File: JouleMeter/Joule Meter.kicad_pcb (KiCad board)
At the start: 4 copper layers, 153.8 x 95 mm, 83 parts, among them J1 XT60-M, J2 XT60-M, J3 22035035, J4 22035035, J5 M22-7130442, U1 LMR36510, U3 INA240A1PW, U4 ADS1118IDGS-Q1, U5 MCP6286T-E/OT1, U6 MCP2562

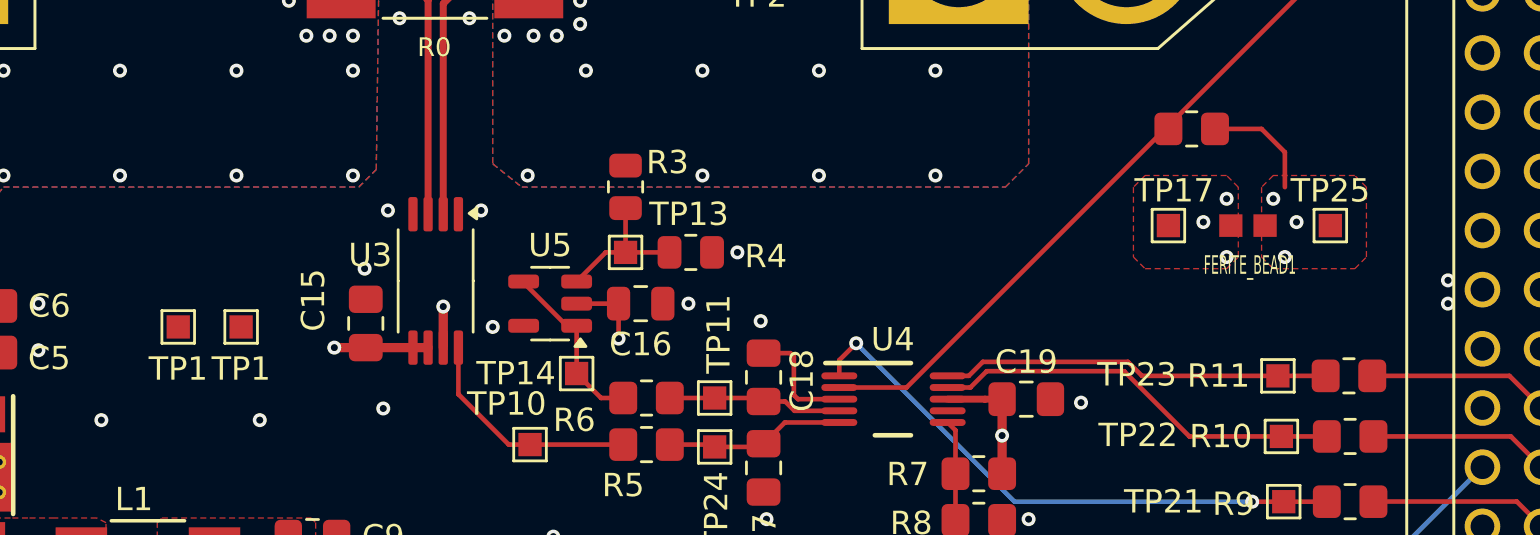
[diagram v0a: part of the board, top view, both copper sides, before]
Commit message: added two new caps next to ferrite bead
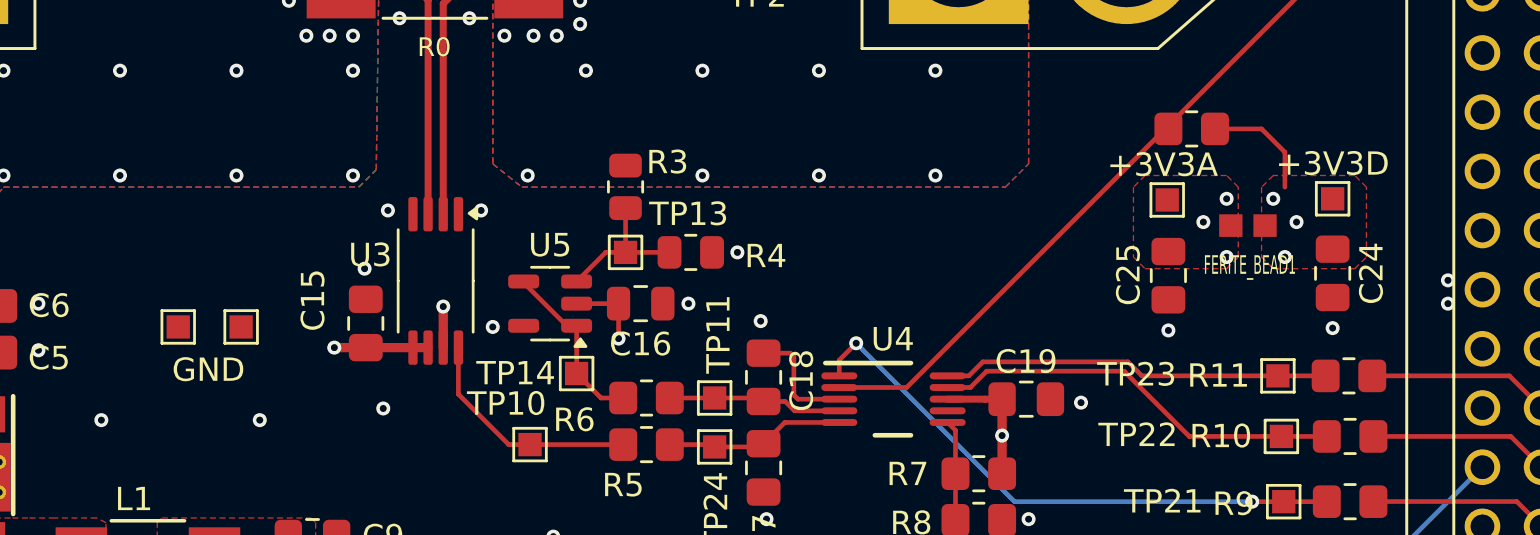
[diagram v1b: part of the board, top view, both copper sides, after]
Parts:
- added C24: 0.1uF, Capacitor_SMD:C_0805_2012Metric_Pad1.18x1.45mm_HandSolder, F.Cu at (137.1, 63.7)
- added C25: 0.1uF, Capacitor_SMD:C_0805_2012Metric_Pad1.18x1.45mm_HandSolder, F.Cu at (130.0, 63.8)
- moved +3V3D 1.15 mm to (137.1, 60.5)
- moved +3V3A 1.10 mm to (129.9, 60.5)
- renumbered TP17 to +3V3A, TP25 to +3V3D, TP1 to GND
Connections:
- C1 pad 3: GND -> (no net)
- C1 pad 4: Net-(J1-POS) -> (no net)
- C3 pad 3: Net-(J2-POS) -> (no net)
- C3 pad 4: GND -> (no net)
- U1 pad 10: GND -> (no net)
- U1 pad 11: GND -> (no net)
- U1 pad 12: GND -> (no net)
- U1 pad 13: GND -> (no net)
- U1 pad 14: GND -> (no net)
- U1 pad 15: GND -> (no net)
- U1 pad 16: GND -> (no net)
- U1 pad 17: GND -> (no net)
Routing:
- net GND: vias 171 -> 173

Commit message: Final Touch Up, Silk Screen
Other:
- board text added: "CAN-N"
- board text added: "CAN-P"
- board text added: "High Power Joulemeter (w/Shunt Resistor) May 2026 University of California, Los Angeles Designed By Sergio Gonzalez"
- board text added: "Special Thanks to: Soloman Ta Edwin Tang For mentoring me in LV, 2025-2026."
- board text removed: "High Power Joulemeter (w/Current Sense) 12/26/2025 University of California, Los Angeles Designed By Sergio Gonzalez"
